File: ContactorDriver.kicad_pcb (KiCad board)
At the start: 2 copper layers, 37 x 49 mm, 32 parts, among them J1 PowerConn, J2 DashboardConnA, J3 ContactorAConn, J4 FanConn1, J5 FanConn2, J6 DashboardConnB, J7 ContactorBConn, J8 FanConn3, Q1 IRLML0030TRPbF, Q2 IRLML0030TRPbF, Q3 IRLML0030TRPbF

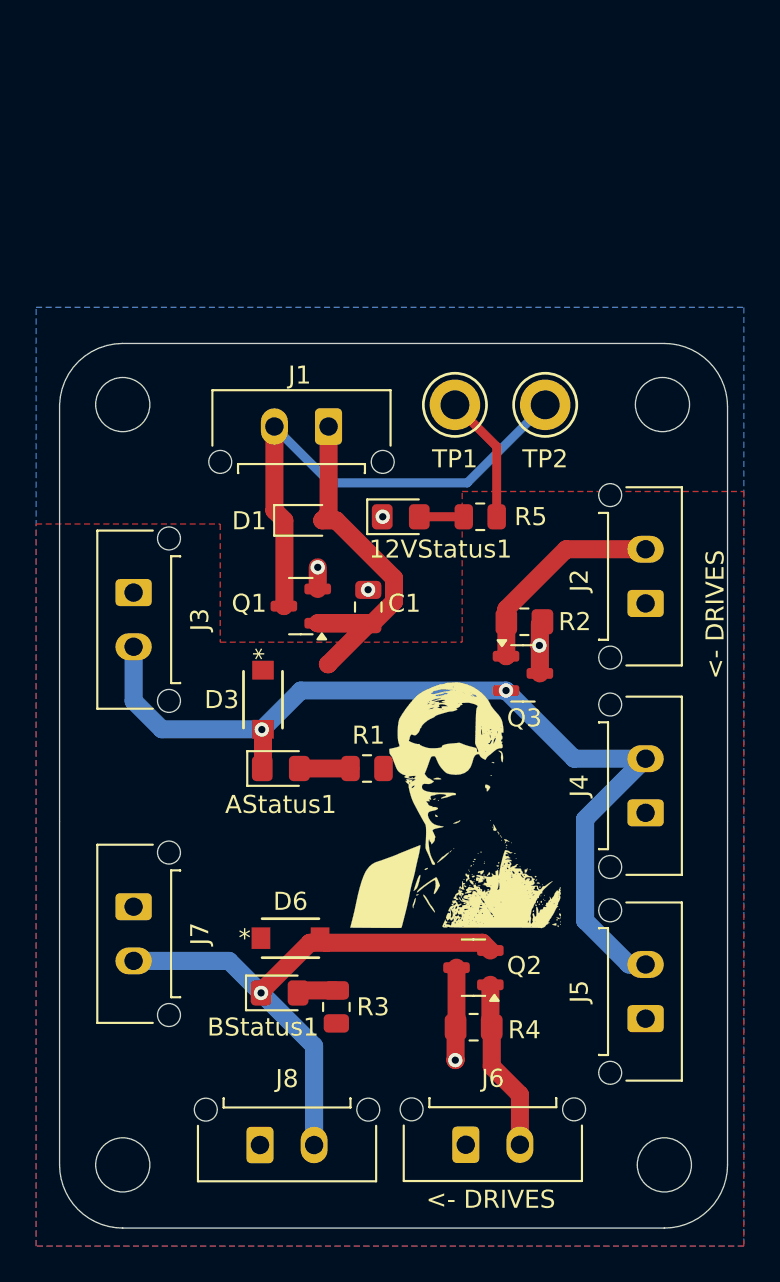
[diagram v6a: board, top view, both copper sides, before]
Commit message: layout fixes
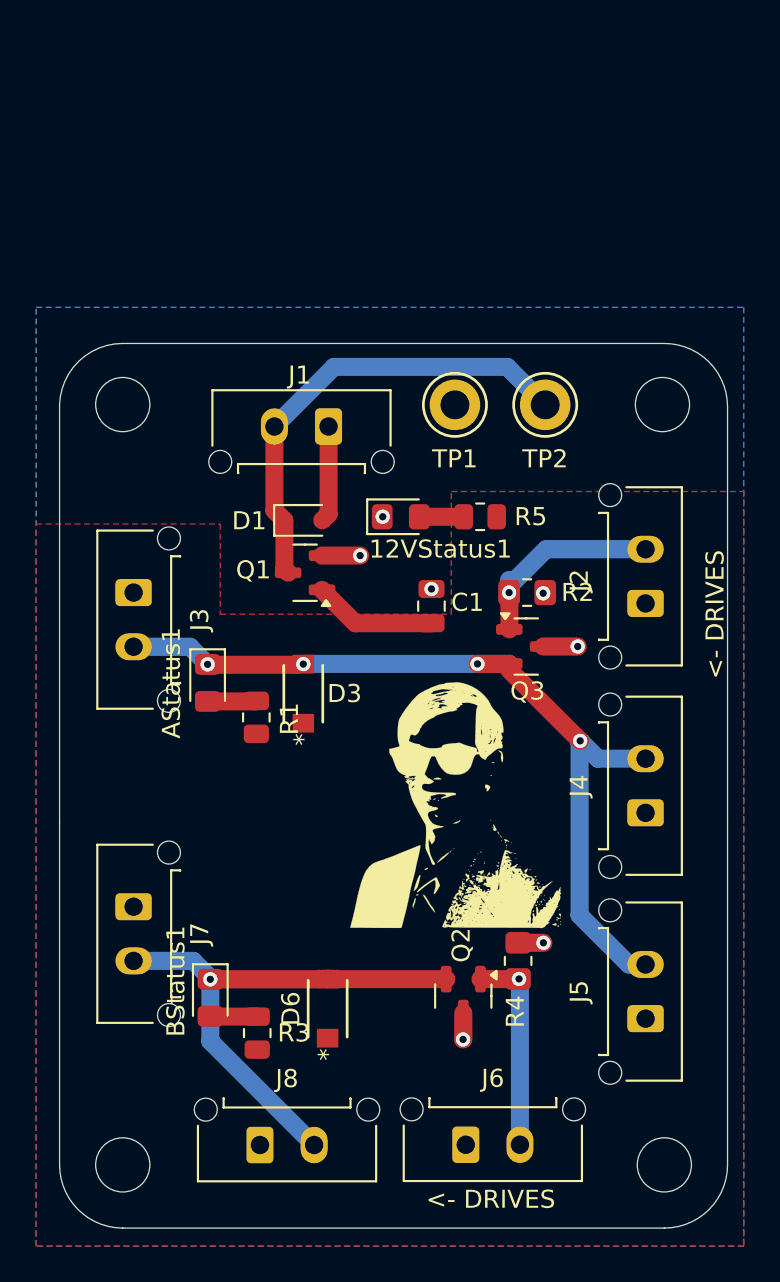
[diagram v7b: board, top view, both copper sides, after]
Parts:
- moved R1 6.75 mm to (107.5, 84.4), turned to -90 degrees
- moved AStatus1 6.24 mm to (104.8, 82.4), turned to -90 degrees
- moved R3 4.62 mm to (107.6, 101.8)
- moved R4 4.42 mm to (122.0, 97.8), turned to -90 degrees
- moved D6 4.42 mm to (111.5, 100.5), turned to 90 degrees
- moved BStatus1 3.85 mm to (105.0, 99.9), turned to -90 degrees
- moved C1 3.50 mm to (117.2, 78.2)
- moved D3 2.26 mm to (110.1, 83.0), turned to 90 degrees
- moved Q1 1.87 mm to (110.2, 76.3)
- moved Q2 1.67 mm to (119.0, 99.8), turned to -90 degrees
- moved R2 1.62 mm to (122.5, 77.4)
- moved Q3 1.50 mm to (122.5, 80.4)
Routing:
- net +12V: track 29.8 -> 12.2 mm
- net /CONTACTOR_A_V-: track 51.5 -> 45.0 mm, vias 2 -> 4
- net Net-(D1-A1): track 28.3 -> 25.7 mm
- net GND: track 9.29 -> 6.89 mm, vias 5 -> 7
- net /CONTACTOR_B_V-: track 31.5 -> 29.3 mm
- net Net-(J6-Pin_2): track 9.54 -> 11.3 mm, vias 0 -> 1
- net Net-(J2-Pin_2): track 11.7 -> 11.2 mm, vias 0 -> 1

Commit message: Fixed warnings
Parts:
- renumbered 12VStatus1 to 12V1
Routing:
- net +12V: track 12.2 -> 0.00 mm
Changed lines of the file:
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@@
 	(net 2 "GND")
 	(net 3 "Net-(D1-A1)")
-	(net 4 "Net-(12VStatus1-A)")
+	(net 4 "Net-(12V1-A)")
 	(net 5 "Net-(AStatus1-A)")
 	(net 6 "/CONTACTOR_A_V-")
@@
 		(tags "SOT TO_SOT_SMD")
 		(property "Reference" "Q2"
-			(at -2.8218 0.109 90)
+			(at 0.348 2.9665 180)
 			(layer "F.SilkS")
 			(effects
@@
 		(tags "resistor handsolder")
 		(property "Reference" "R2"
-			(at -2.794 0 180)
+			(at -0.354 1.686 180)
 			(layer "F.SilkS")
 			(effects
@@
 		(at 110.105 83.04 90)
 		(property "Reference" "D3"
-			(at 0 2.286 360)
+			(at 0 2.286 0)
 			(layer "F.SilkS")
 			(effects
@@
 		)
 		(property "Value" "V2F22HM3/H"
-			(at 0 0 270)
+			(at 0 0 -90)
 			(layer "F.Fab")
 			(effects
@@
 		)
 		(fp_text user "*"
-			(at -2.54 0 270)
+			(at -2.54 0 -90)
 			(layer "F.SilkS")
 			(effects
@@
 		)
 		(fp_text user "*"
-			(at -2.54 0 270)
+			(at -2.54 0 -90)
 			(layer "F.SilkS")
 			(hide yes)
@@
 		)
 		(fp_text user "0.047in/1.194mm"
-			(at 4.3688 2 270)
+			(at 4.3688 2 -90)
 			(layer "Dwgs.User")
 			(hide yes)
@@
 		)
 		(fp_text user "0.041in/1.041mm"
-			(at 0.6383 3.975 360)
+			(at 0.6383 3.975 0)
 			(layer "Dwgs.User")
 			(hide yes)
@@
 		)
 		(fp_text user "Copyright 2016 Accelerated Designs. All rights reserved."
-			(at 0 0 270)
+			(at 0 0 -90)
 			(layer "Cmts.User")
 			(hide yes)
@@
 		)
 		(fp_text user "*"
-			(at -1.1938 0 270)
+			(at -1.1938 0 -90)
 			(layer "F.Fab")
 			(hide yes)
@@
 		)
 		(fp_text user "*"
-			(at -1.1938 0 270)
+			(at -1.1938 0 -90)
 			(layer "F.Fab")
 			(hide yes)
@@
 		(tags "connector Molex Micro-Fit_3.0 vertical")
 		(property "Reference" "J7"
-			(at 1.5 -3.67 -90)
+			(at 7.584 -0.056 0)
 			(layer "F.SilkS")
 			(effects
@@
 		(tags "connector Molex Micro-Fit_3.0 vertical")
 		(property "Reference" "J3"
-			(at 1.5 -3.67 -90)
+			(at 7.458 -0.056 0)
 			(layer "F.SilkS")
 			(effects
@@
 		(tags "LED handsolder")
 		(property "Reference" "BStatus1"
-			(at -0.9187 1.9 90)
+			(at -5.589 -0.124 270)
 			(layer "F.SilkS")
 			(effects
@@
 		(tags "resistor")
 		(property "Reference" "R1"
-			(at 0.08 -1.838 90)
+			(at 2.8315 -0.114 180)
 			(layer "F.SilkS")
 			(effects
@@
 		(descr "LED SMD 0805 (2012 Metric), square (rectangular) end terminal, IPC_7351 nominal, (Body size source: https://docs.google.com/spreadsheets/d/1BsfQQcO9C6DZCsRaXUlFlo91Tg2WpOkGARC1WS5S8t0/edit?usp=sharing), generated with kicad-footprint-generator")
 		(tags "LED handsolder")
-		(property "Reference" "12VStatus1"
-			(at 2.2 1.8 0)
+		(property "Reference" "12V1"
+			(at 0.496 2.006 0)
 			(layer "F.SilkS")
 			(effects
@@
 			(layers "F.Cu" "F.Paste" "F.Mask")
 			(roundrect_rratio 0.217391)
-			(net 4 "Net-(12VStatus1-A)")
+			(net 4 "Net-(12V1-A)")
 			(pinfunction "A")
 			(pintype "passive")
@@
 			(layers "F.Cu" "F.Paste" "F.Mask")
 			(roundrect_rratio 0.243902)
-			(net 4 "Net-(12VStatus1-A)")
+			(net 4 "Net-(12V1-A)")
 			(pintype "passive")
 		)
@@
 		(tags "resistor")
 		(property "Reference" "R3"
-			(at 0 -2.032 0)
+			(at -2.972 -0.064 0)
 			(layer "F.SilkS")
 			(effects
@@
 		(at 111.455 100.49 90)
 		(property "Reference" "D6"
-			(at 0 -2.032 270)
+			(at 0 -2.032 -90)
 			(layer "F.SilkS")
 			(effects
@@
 		)
 		(property "Value" "V2F22HM3/H"
-			(at 0 0 270)
+			(at 0 0 -90)
 			(layer "F.Fab")
 			(effects
@@
 		)
 		(fp_text user "*"
-			(at -2.54 0 270)
+			(at -2.54 0 -90)
 			(layer "F.SilkS")
 			(effects
@@
 		)
 		(fp_text user "*"
-			(at -2.54 0 270)
+			(at -2.54 0 -90)
 			(layer "F.SilkS")
 			(hide yes)
@@
 		)
 		(fp_text user "0.041in/1.041mm"
-			(at -1.6383 -3.8608 270)
+			(at -1.6383 -3.8608 -90)
 			(layer "Dwgs.User")
 			(hide yes)
@@
 		)
 		(fp_text user "0.047in/1.194mm"
-			(at 4.3688 0 270)
+			(at 4.3688 0 -90)
 			(layer "Dwgs.User")
 			(hide yes)
@@
 		)
 		(fp_text user "Copyright 2016 Accelerated Designs. All rights reserved."
-			(at 0 0 270)
+			(at 0 0 -90)
 			(layer "Cmts.User")
 			(hide yes)
@@
 		)
 		(fp_text user "*"
-			(at -1.1938 0 270)
+			(at -1.1938 0 -90)
 			(layer "F.Fab")
 			(hide yes)
@@
 		)
 		(fp_text user "*"
-			(at -1.1938 0 270)
+			(at -1.1938 0 -90)
 			(layer "F.Fab")
 			(hide yes)
@@
 		(tags "LED handsolder")
 		(property "Reference" "AStatus1"
-			(at 0 2 90)
+			(at -5.67 -0.02 90)
 			(layer "F.SilkS")
 			(effects
@@
 	)
 	(segment
-		(start 111.1425 77.29)
-		(end 112.9925 79.14)
-		(width 1)
-		(layer "F.Cu")
-		(net 1)
-	)
-	(segment
-		(start 111.505 68.24)
-		(end 111.505 73.09)
-		(width 1)
-		(layer "F.Cu")
-		(net 1)
-	)
-	(segment
-		(start 112.9925 79.14)
-		(end 117.205 79.14)
-		(width 1)
-		(layer "F.Cu")
-		(net 1)
-	)
-	(segment
-		(start 111.505 73.09)
-		(end 111.155 73.44)
-		(width 1)
-		(layer "F.Cu")
-		(net 1)
-	)
-	(segment
 		(start 118.9675 100.7275)
 		(end 118.9675 102.1775)
@@
 		(polygon
 			(pts
-				(xy 95.305 73.64) (xy 105.505 73.64) (xy 105.505 78.636) (xy 118.305 78.64) (xy 118.305 78.639821)
-				(xy 118.305 71.84) (xy 134.505 71.84) (xy 134.505 113.64) (xy 95.305 113.64)
+				(xy 95.305 61.702) (xy 105.505 61.702) (xy 105.505 61.618) (xy 118.305 61.622) (xy 118.287 61.784)
+				(xy 118.305 61.68) (xy 134.505 61.68) (xy 134.505 113.64) (xy 95.305 113.64)
 			)
 		)
